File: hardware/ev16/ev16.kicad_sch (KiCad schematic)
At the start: 165 parts, among them CN1 Conn_05x02_Female, CN2 PJ-242, J1 USB_C_Receptacle, J10 Conn_02x04_Odd_Even, J11 Conn_02x05_Counter_Clockwise, J2 Conn_01x02_Socket, J3 AudioJack4, J4 Conn_01x18_MountingPin, J5 Conn_02x03_Odd_Even, J7 Conn_02x05_Counter_Clockwise, J8 Conn_02x05_Counter_Clockwise, J9 Conn_02x05_Counter_Clockwise, Q1 2N7002, SW1 SW_SPDT, SW2 SW_Push, SW3 SW_Push, SW4 SW_Push, SW5 SW_Push, U1 BQ21040DBV, U10 STM32F405RGTx, U2 USBLC6-2P6, U3 STM32F072CBTx, U4 CH340C, U5 TPS63060, U6 WM8960CGEFL/RV, U7 ESP32-S3-WROOM-1, U8 M24C02-RMN6TP, U9 BM14B(0.8)-24DS-0.4V(53), Y1 Crystal_GND24

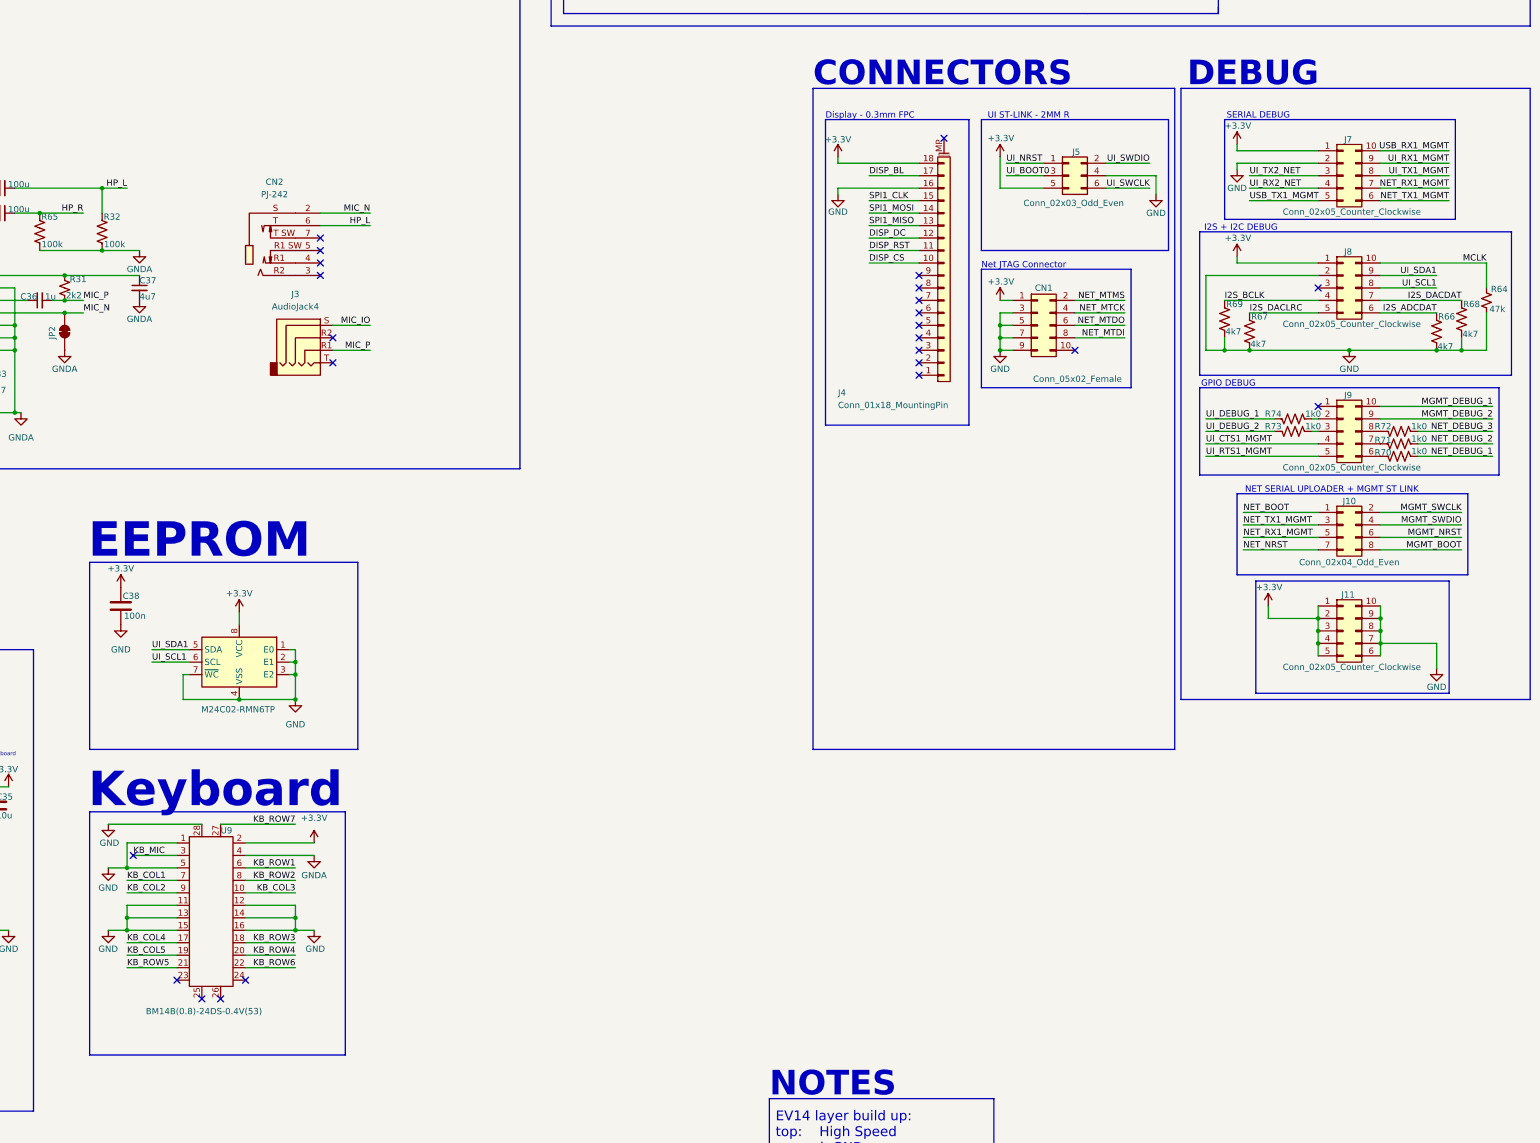
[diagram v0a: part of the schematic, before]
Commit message: Added a connector for mgmt swdio, added spi to dev board
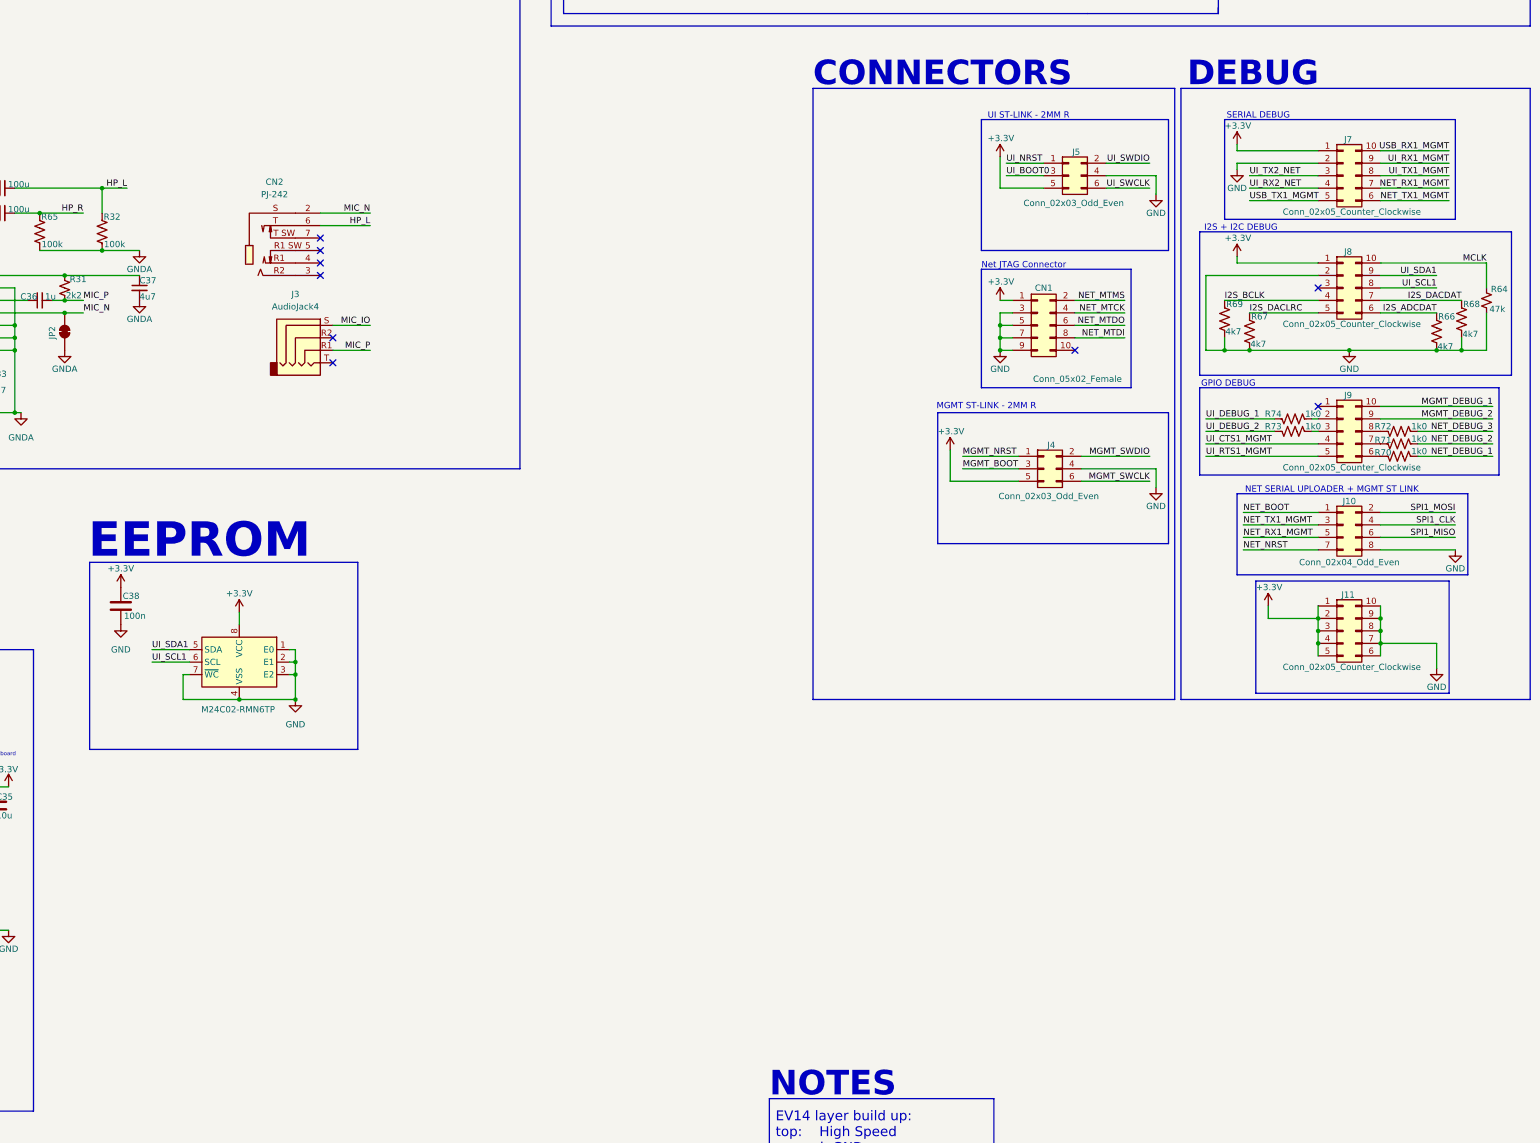
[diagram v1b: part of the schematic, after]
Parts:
- removed J4: Conn_01x18_MountingPin, symbol Connector_Generic_MountingPin:Conn_01x18_MountingPin
- removed U9: BM14B(0.8)-24DS-0.4V(53), Hactar_Footprints:BM14B(0.B)-24DS-0.4V(53), symbol Hactar_Symbols:BM14B(0.8)-24DS-0.4V(53)
- added J4: Conn_02x03_Odd_Even, Hactar_Footprints:HDR-SMD_6P-P2.54-V-M-R2-C3-LS7.5-2, symbol Connector_Generic:Conn_02x03_Odd_Even
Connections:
- net +3.3V: now also J4.5 (Pin_5)
- net GND: now also J10.8 (Pin_8), J4.4 (Pin_4)
- net MGMT_BOOT: now also J4.3 (Pin_3); no longer J10.8 (Pin_8)
- net MGMT_NRST: now also J4.1 (Pin_1); no longer J10.6 (Pin_6)
- net MGMT_SWCLK: now also J4.6 (Pin_6); no longer J10.2 (Pin_2)
- net MGMT_SWDIO: now also J4.2 (Pin_2); no longer J10.4 (Pin_4)
- net SPI1_CLK: now also J10.4 (Pin_4)
- net SPI1_MISO: now also J10.6 (Pin_6)
- net SPI1_MOSI: now also J10.2 (Pin_2)
- no-connect marks 49 -> 34
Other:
- note added: "MGMT ST-LINK - 2MM R"
- note removed: "Display - 0.3mm FPC"
- note removed: "Keyboard"

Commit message: added volume buttons, changed schematic for buttons to be a 4 lead variant, change led sch to built in ones, picked horizontal leds. Removed one mgmt led. Moved debuggers to dev board. Removed keyboard and screen connectors. Rotated battery connector, added cutout for battery connector. Changed rst and boot buttons to vertical buttons and moved them. Cleaned up usb-c area
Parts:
- removed D4, D5, D6, D8: NH-B1515RGBA-HF, Hactar_Footprints:LED-ARRAY-SMD_4P-L1.6-W1.5-TL_NH-B1515RGBA, symbol Hactar_Symbols:NH-B1515RGBA-HF
- removed H1: MountingHole, MountingHole:MountingHole_2.7mm_M2.5, symbol Mechanical:MountingHole
- removed J10: Conn_02x04_Odd_Even, Hactar_Footprints:HDR-SMD_8P-P2.54-V-M-R2-C4-LS7.4, symbol Connector_Generic:Conn_02x04_Odd_Even
- removed R17: 180R, Resistor_SMD:R_0402_1005Metric, symbol Device:R_US
- removed R23, R24: 150R, Resistor_SMD:R_0402_1005Metric, symbol Device:R_US
- removed R47, R48, R51, R52, R53: 680R, Resistor_SMD:R_0402_1005Metric, symbol Device:R_US
- added C49, C50: 100n, Capacitor_SMD:C_0402_1005Metric, symbol Device:C_Small
- added D5: LED_BGAR, Hactar_Footprints:LED-ARRAY-SMD_4P-L1.6-W1.5-TL_NH-B1515RGBA, symbol Device:LED_RABG
- added D7, D9: LED_BGAR, Hactar_Footprints:LED-ARRAY-SMD_HS-1204-RGB, symbol Device:LED_BGAR
- added J6: Conn_02x05_Counter_Clockwise, Hactar_Footprints:HDR-SMD_10P-P2.54-V-F-R2-C5-LS7.1-1, symbol Connector_Generic:Conn_02x05_Counter_Clockwise
- added R17, R24: 1k0, Resistor_SMD:R_0402_1005Metric, symbol Device:R_Small_US
- added R23, R37: 4k7, Resistor_SMD:R_0402_1005Metric, symbol Device:R_Small_US
- added SW6, SW7: SW_Push, Hactar_Footprints:SW-SMD_SHOU_TS36CA-0.6, symbol Switch:SW_Push
- SW2, SW3: footprint Hactar_Footprints:SW-SMD_SHOU_TS36CA-0.6 -> Hactar_Footprints:KEY-SMD_4P-L4.2-W3.2-P2.20-LS4.6; symbol Switch:SW_Push -> Hactar_Symbols:SW_Push_4C; JLCPCB Part # C2906288 -> C139797
- SW4, SW5: footprint Hactar_Footprints:SW-SMD_L6.0-W6.0-LS6.6 -> Hactar_Footprints:SW-SMD_4P-L5.1-W5.1-P3.70-LS6.5-TL_H1.5; symbol Switch:SW_Push -> Hactar_Symbols:SW_Push_4C; JLCPCB Part # C97448 -> C318884
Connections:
- net KB_COL1 is gone; now on an unnamed net: R43.2
- net +3.3V: now also SW2.2, SW4.2, SW5.2, D5.2 (A), D7.3 (A), D9.3 (A), SW6.1, SW7.1
- net GND: now also SW3.3, SW3.4, C49.2, C50.2, J6.5 (Pin_5), J6.6 (Pin_6), J6.7 (Pin_7), R23.1, R37.1; no longer SW3.2
- net MGMT_BOOT: now also SW2.3, SW2.4; no longer SW2.2
- net MGMT_NRST: now also SW3.2
- net NET_BOOT: now also J6.1 (Pin_1)
- net NET_NRST: now also J6.4 (Pin_4)
- net NET_RX1_MGMT: now also J6.3 (Pin_3)
- net NET_TX1_MGMT: now also J6.2 (Pin_2)
- net SPI1_CLK: now also J6.9 (Pin_9)
- net SPI1_MISO: now also J6.8 (Pin_8)
- net SPI1_MOSI: now also J6.10 (Pin_10)
- net at C47.1, R58.2, R62.2: now also SW5.3, SW5.4; no longer SW5.2
- net at R59.2: now also D9.4 (RK)
- net at R56.2: now also D9.1 (BK)
- net at R60.2: now also D9.2 (GK)
- net at R33.2: now also D7.1 (BK)
- net at R34.2: now also D7.4 (RK)
- net at R35.2: now also D7.2 (GK)
- net at R20.1: now also D5.1 (RK)
- net at R15.1: now also D5.3 (BK)
- net at R21.1: now also D5.4 (GK)
- net VOLUME-: now reaches U10.36 (PB15)
- net VOLUME-: now also R24.1
- net at C46.1, R57.2, R61.2: now also SW4.3, SW4.4; no longer SW4.2
- net DISP_BL: no longer names the net of U10.3 (PC14)
- net DISP_CS: no longer names the net of U10.61 (PB8)
- net DISP_DC: no longer names the net of U10.62 (PB9)
- net DISP_RST: no longer names the net of U10.2 (PC13)
- net KB_ROW1: no longer names the net of U10.33 (PB12)
- net KB_ROW2 renamed VOLUME+
- net VOLUME+: now also R17.1
- net KB_ROW3: no longer names the net of U10.39 (PC8)
- net KB_ROW4: no longer names the net of U10.41 (PA8)
- net KB_ROW5: no longer names the net of U10.26 (PB0)
- net KB_ROW6: no longer names the net of U10.27 (PB1)
- net KB_ROW7: no longer names the net of R42.2, U10.30 (PB11)
- net LEDB_B: no longer names the net of U3.28 (PB15)
- net LEDB_G: no longer names the net of U3.42 (PB6)
- net LEDB_R: no longer names the net of U3.18 (PB0)
- new net: C50.1, R24.2, R37.2, SW7.2
- new net: C49.1, R17.2, R23.2, SW6.2
- no-connect marks 34 -> 49
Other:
- note added: "NET SERIAL UPLOADER + SPI"
- note added: "Programmers"
- note added: "Volume"
- note removed: "CONNECTORS"
- note removed: "NET SERIAL UPLOADER + MGMT ST LINK"
- moved on the sheet: C17, C18, C46, C47, CN1, J11, J4, J5, Q1, R15, R20, R21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

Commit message: feat: finish tracing all chips, missing dev board
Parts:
- removed R3: 4k7, Resistor_SMD:R_0402_1005Metric, symbol Device:R_US
- added R47: 0R1, Resistor_SMD:R_0603_1608Metric, symbol Device:R_US
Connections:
- net +3.3V: now also R47.1; no longer L1.1
- net BATTERY_MON: now also U3.18 (PB0); no longer U10.24 (PC4)
- net NET_RX1_MGMT: no longer J7.7 (Pin_7)
- net NET_TX1_MGMT: no longer J7.6 (Pin_6)
- net CHG_FB: now reaches U3.19 (PB1)
- net CHG_FB: now also D1.2 (A), R11.2
- new net: L1.1, R47.2
- no-connect marks 49 -> 51
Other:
- moved on the sheet: C10, C11, J6, L1, NT1

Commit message: finish wiring up the remaining connections between chips and dev board. Added charging detect wiring
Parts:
- added J10: Conn_01x03_Pin, Connector_PinSocket_2.54mm:PinSocket_1x03_P2.54mm_Vertical_SMD_Pin1Left, symbol Connector:Conn_01x03_Pin
- added Q2: 2N7002, Package_TO_SOT_SMD:SOT-23, symbol Transistor_FET:2N7002
- added R3: 47k, Resistor_SMD:R_0402_1005Metric, symbol Device:R_Small_US
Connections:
- net +3.3V: now also R3.2
- net CHG_FB: now also Q2.3 (D), R3.1; no longer D1.2 (A), R11.2
- net GND: now also Q2.2 (S)
- net GNDA: now also J10.3 (Pin_3)
- net HP_L: now also J10.1 (Pin_1)
- net MIC_P: now also J10.2 (Pin_2)
- net at D1.1 (K), U1.3 (~{CHG}): now also Q2.1 (G)
- new net: D1.2 (A), R11.2
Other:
- note added: "Audio Debug"
- moved on the sheet: C12, D1, D2, D3, J2, R11, R6

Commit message: chore: clean up file versions and dates
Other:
- title: EV15 FINN BERG & BRETT REGNIER -> EV16 FINN BERG & BRETT REGNIER
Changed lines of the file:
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@@
 	(paper "A2")
 	(title_block
-		(title "EV15 FINN BERG & BRETT REGNIER")
-		(date "2025-07-25")
-		(rev "EV15")
+		(title "EV16 FINN BERG & BRETT REGNIER")
+		(date "2025-11-26")
+		(rev "EV16")
 		(company "CISCO SYSTEMS INC")
 	)
